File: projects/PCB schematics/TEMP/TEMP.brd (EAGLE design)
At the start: 58.4 x 54.6 mm, 17 parts, among them J1 SAMTEC-TFM-120-02-X-D-LCJ, X1 5566-4, X2 5566-4, X3 5566-2, X4 5566-6

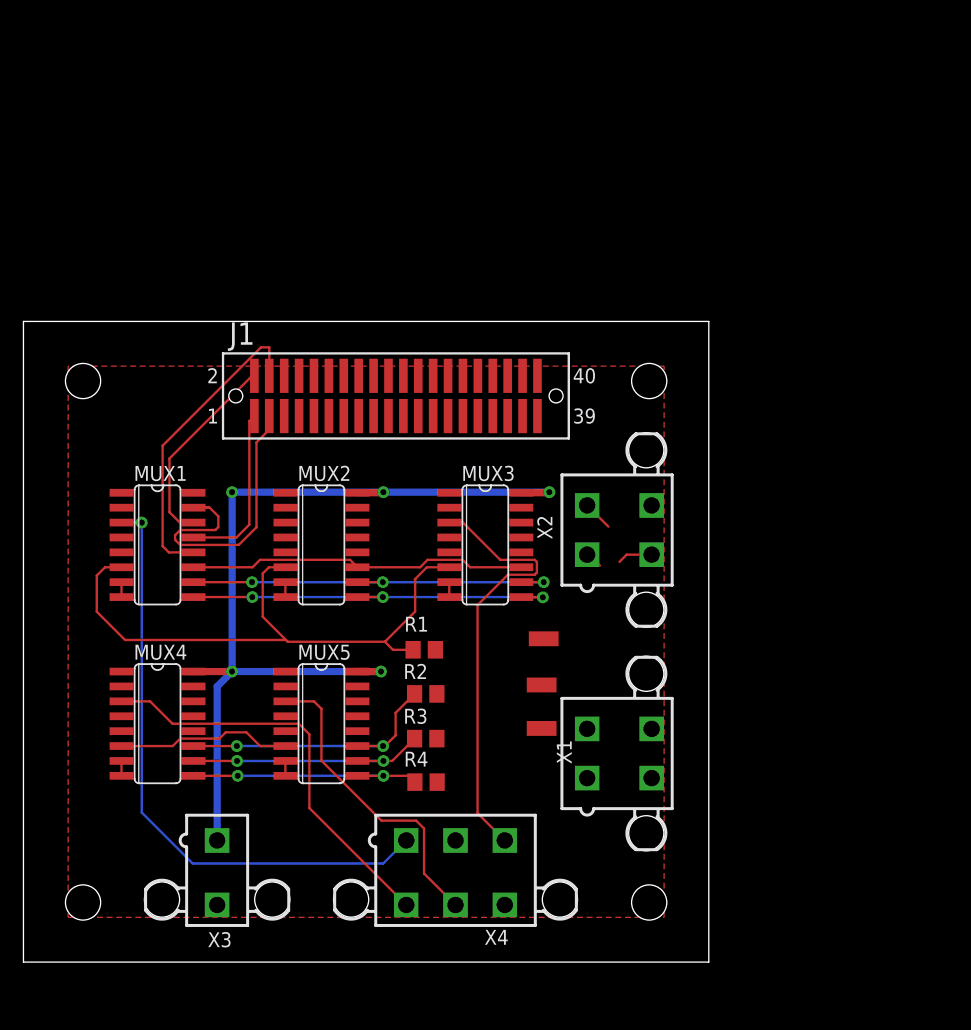
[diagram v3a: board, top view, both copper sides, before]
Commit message: TEMP - Energus components added in.
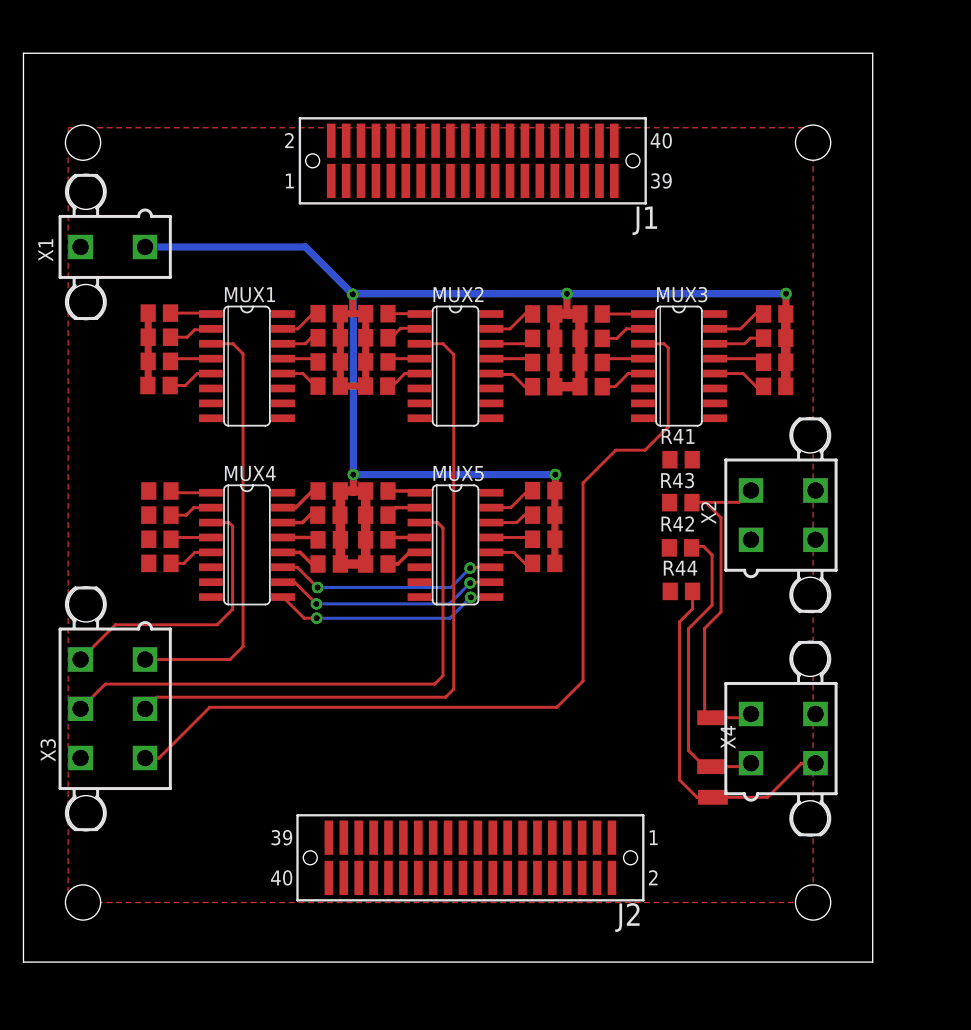
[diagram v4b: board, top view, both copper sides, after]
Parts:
- added J2: SAMTEC-TFM-120-02-X-D-LCJ, SAMTEC-TFM-120-02-X-D-LC:SAMTEC-TFM-120-02-X-D-LC
- added R10, R11, R12, R13, R14, R15, R16, R17, R18, R19, R20, R21, R22, R23, R24, R25, R26, R27, R28, R29, R30, R31, R32, R33, R34, R35, R36, R37, R38, R39, R40, R5, R6, R7, R8, R9: 680, rcl:R0805
- added R41, R42, R43, R44: 50k, rcl:R0805
- R1, R2, R3, R4: value 50k -> 680
- X1: value 5566-4 -> 5566-2; device con-molex:5566-4 -> con-molex:5566-2
- X3: value 5566-2 -> 5566-6; device con-molex:5566-2 -> con-molex:5566-6
- X4: value 5566-6 -> 5566-4; device con-molex:5566-6 -> con-molex:5566-4
- moved X1 61.1 mm to (7.62, 61.0), turned to 90 degrees
- moved R3 37.1 mm to (26.1, 55.3)
- moved R4 34.8 mm to (26.1, 49.1)
- moved R2 31.4 mm to (26.1, 53.2)
- moved X4 30.2 mm to (64.8, 19.1), turned to 270 degrees
- moved R1 25.8 mm to (26.1, 51.2)
- moved MUX3 22.5 mm to (55.9, 50.8)
- moved J1 21.1 mm to (38.3, 68.3)
- moved MUX5 19.1 mm to (36.8, 35.6)
- moved MUX2 19.0 mm to (36.8, 50.8)
- moved SH1 18.0 mm to (58.7, 16.7), turned to 180 degrees
- moved MUX4 17.0 mm to (19.1, 35.6)
- moved MUX1 17.0 mm to (19.1, 50.8)
- moved X3 16.6 mm to (7.62, 21.6), turned to 90 degrees
- moved SH3 15.7 mm to (58.8, 14.0), turned to 180 degrees
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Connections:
- net CS_A_IN: now also R42.2; no longer R2.2
- net CS_A_OUT: now also X4.1; no longer X1.1
- net CS_B_IN: now also R43.2; no longer R3.2
- net CS_B_OUT: now also X4.2; no longer X1.2
- net CS_C_IN: now also R44.2; no longer R4.2
- net CS_C_OUT: now also X4.3; no longer X1.3
- net GND: now also J1.10, J1.12, J1.14, J1.16, J1.18, J1.2, J1.20, J1.22, J1.24, J1.26, J1.28, J1.30, J1.32, J1.34, J1.36, J1.38, J1.4, J1.40, J1.6, J1.8, J2.10, J2.12, J2.14, J2.16, J2.18, J2.2, J2.20, J2.22, J2.24, J2.26, J2.28, J2.30, J2.32, J2.34, J2.36, J2.38, J2.4, J2.40, J2.6, J2.8, R41.1, R42.1, R43.1, R44.1, X1.2; no longer R1.1, R2.1, R3.1, R4.1, X3.2
- net INH: now also R41.2; no longer R1.2
- net TEMP1: now also R1.2
- net TEMP10: now also J1.19, R10.2; no longer J1.10
- net TEMP11: now also J1.21, R11.2; no longer J1.11
- net TEMP12: now also J1.23, R12.2; no longer J1.12
- net TEMP13: now also J1.25, R13.2; no longer J1.13
- net TEMP14: now also J1.27, R14.2; no longer J1.14
- net TEMP15: now also J1.29, R15.2; no longer J1.15
- net TEMP16: now also J1.31, R16.2; no longer J1.16
- net TEMP17: now also J1.33, R17.2; no longer J1.17
- net TEMP18: now also J1.35, R18.2; no longer J1.18
- net TEMP19: now also J1.37, R19.2; no longer J1.19
- net TEMP2: now also J1.3, R2.2; no longer J1.2
- net TEMP20: now also J1.39, R20.2; no longer J1.20
- net TEMP21: now also J2.1, R21.2; no longer J1.21
- net TEMP22: now also J2.3, R22.2; no longer J1.22
- net TEMP23: now also J2.5, R23.2; no longer J1.23
- net TEMP24: now also J2.7, R24.2; no longer J1.24
- net TEMP25: now also J2.9, R25.2; no longer J1.25
- net TEMP26: now also J2.11, R26.2; no longer J1.26
- net TEMP27: now also J2.13, R27.2; no longer J1.27
- net TEMP28: now also J2.15, R28.2; no longer J1.28
- net TEMP29: now also J2.17, R29.2; no longer J1.29
- net TEMP3: now also J1.5, R3.2; no longer J1.3
- net TEMP30: now also J2.19, R30.2; no longer J1.30
- net TEMP31: now also J2.21, R31.2; no longer J1.31
- net TEMP32: now also J2.23, R32.2; no longer J1.32
- net TEMP33: now also J2.25, R33.2; no longer J1.33
- net TEMP34: now also J2.27, R34.2; no longer J1.34
- net TEMP35: now also J2.29, R35.2; no longer J1.35
- net TEMP36: now also J2.31, R36.2; no longer J1.36
- net TEMP37: now also J2.33, R37.2; no longer J1.37
- net TEMP38: now also J2.35, R38.2; no longer J1.38
- net TEMP39: now also J2.37, R39.2; no longer J1.39
- net TEMP4: now also J1.7, R4.2; no longer J1.4
- net TEMP40: now also J2.39, R40.2; no longer J1.40
- net TEMP5: now also J1.9, R5.2; no longer J1.5
- net TEMP6: now also J1.11, R6.2; no longer J1.6
- net TEMP7: now also J1.13, R7.2; no longer J1.7
- net TEMP8: now also J1.15, R8.2; no longer J1.8
- net TEMP9: now also J1.17, R9.2; no longer J1.9
- net TEMP_OUT1: now also X3.1; no longer X4.1
- net TEMP_OUT2: now also X3.2; no longer X4.2
- net TEMP_OUT3: now also X3.3; no longer X4.3
- net TEMP_OUT4: now also X3.4; no longer X4.4
- net TEMP_OUT5: now also X3.5; no longer X4.5
- net VCC: now also R1.1, R10.1, R11.1, R12.1, R13.1, R14.1, R15.1, R16.1, R17.1, R18.1, R19.1, R2.1, R20.1, R21.1, R22.1, R23.1, R24.1, R25.1, R26.1, R27.1, R28.1, R29.1, R3.1, R30.1, R31.1, R32.1, R33.1, R34.1, R35.1, R36.1, R37.1, R38.1, R39.1, R4.1, R40.1, R5.1, R6.1, R7.1, R8.1, R9.1, X1.1; no longer X3.1
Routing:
- net VCC: track 80.5 -> 165.6 mm
- net INH: track 67.2 -> 0.00 mm
- net TEMP_OUT2: track 0.00 -> 58.8 mm
- net TEMP_OUT3: track 37.0 -> 75.2 mm
- net TEMP4: track 26.4 -> 3.43 mm
- net TEMP3: track 25.9 -> 3.52 mm
- net TEMP_OUT5: track 26.5 -> 46.9 mm
- net CS_C_IN: track 58.1 -> 38.6 mm, vias 5 -> 2
- net CS_B_IN: track 59.1 -> 44.3 mm, vias 5 -> 2
- net TEMP_OUT1: track 51.6 -> 36.9 mm, vias 1 -> 0
- net TEMP2: track 17.2 -> 3.20 mm
- net CS_A_IN: track 54.4 -> 40.7 mm
- net TEMP1: track 14.6 -> 3.10 mm
- net TEMP_OUT4: track 35.1 -> 23.8 mm
- net CS_C_OUT: track 0.00 -> 9.31 mm
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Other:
- board size 58.4 x 54.6 mm -> 72.4 x 77.5 mm

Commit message: TEMP - Initial board placement; Horizontal redo.
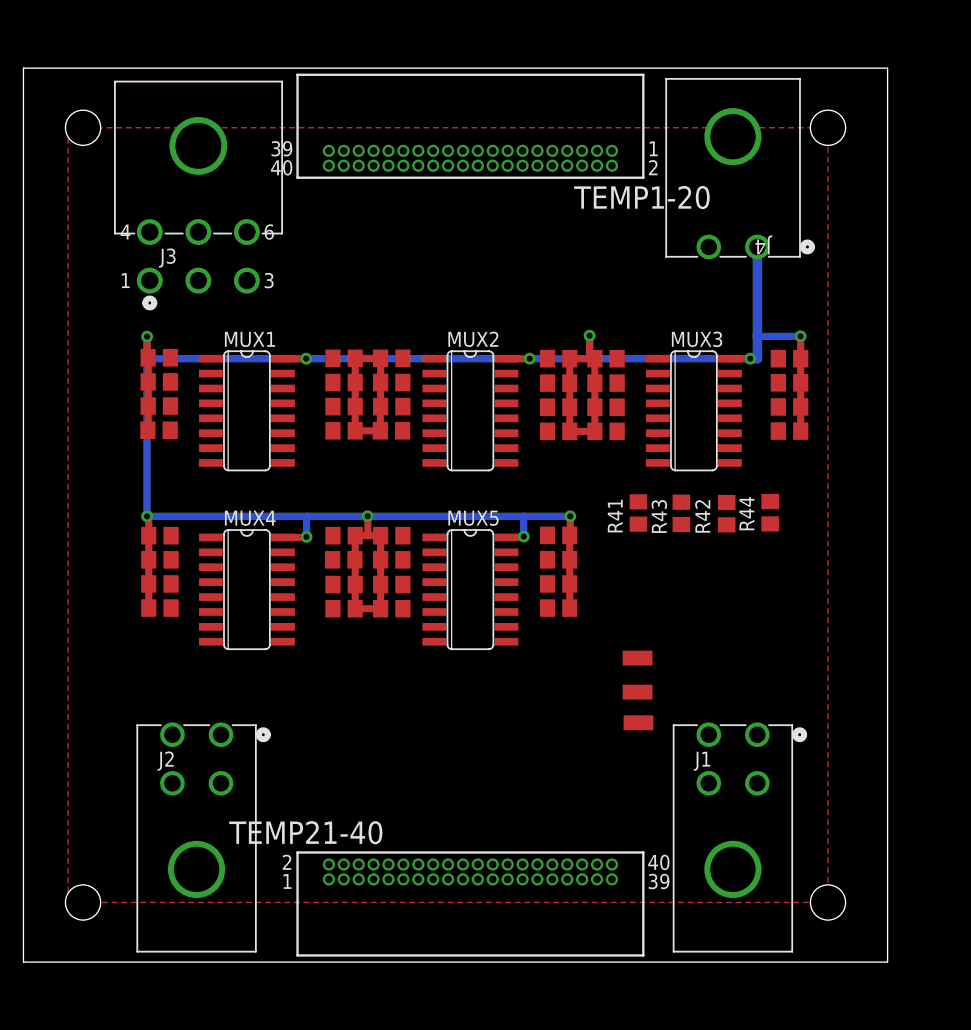
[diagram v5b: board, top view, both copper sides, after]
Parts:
- removed X1: 5566-2, con-molex:5566-2
- removed X2, X4: 5566-4, con-molex:5566-4
- removed X3: 5566-6, con-molex:5566-6
- added J3: 1-770969-0, IowaFormula:CON6_2X3_P163_RAMNL
- added J4: 770966-1, IowaFormula:CONN2_770966-1
- added TEMP1-20, TEMP21-40: SAMTEC-TFM-120-01-X-D-RA, SAMTEC-TFM-120-01-X-D-RA:SAMTEC-TFM-120-01-X-D-RA
- J1, J2: value SAMTEC-TFM-120-02-X-D-LCJ -> 770968-1; device SAMTEC-TFM-120-02-X-D-LC:SAMTEC-TFM-120-02-X-D-LC -> IowaFormula:CONN4_770968-1
- moved J1 56.7 mm to (58.4, 15.2)
- moved J2 26.2 mm to (12.7, 15.2), turned to 0 degrees
- moved R44 10.1 mm to (63.7, 38.3), turned to 90 degrees
- moved SH3 8.98 mm to (52.4, 20.4)
- moved SH1 8.98 mm to (52.3, 23.0)
- moved SH2 8.13 mm to (52.3, 25.9)
- moved R41 5.82 mm to (52.4, 38.3), turned to 90 degrees
- moved R42 4.90 mm to (59.9, 38.2), turned to 90 degrees
- moved MUX5 4.02 mm to (38.1, 31.8)
- moved R12 4.02 mm to (45.6, 45.2)
- moved R33 4.02 mm to (45.6, 32.2)
- moved R34 4.02 mm to (45.6, 34.3)
- moved R35 4.02 mm to (45.6, 36.4)
- moved R1 4.02 mm to (27.3, 47.3)
- moved R13 4.02 mm to (31.4, 51.5)
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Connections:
- net CS_A_IN: now also J1.1; no longer X2.1
- net CS_A_OUT: now also J2.1; no longer X4.1
- net CS_B_IN: now also J1.2; no longer X2.2
- net CS_B_OUT: now also J2.2; no longer X4.2
- net CS_C_IN: now also J1.3; no longer X2.3
- net CS_C_OUT: now also J2.3; no longer X4.3
- net GND: now also J4.2, TEMP1-20.10, TEMP1-20.12, TEMP1-20.14, TEMP1-20.16, TEMP1-20.18, TEMP1-20.2, TEMP1-20.20, TEMP1-20.22, TEMP1-20.24, TEMP1-20.26, TEMP1-20.28, TEMP1-20.30, TEMP1-20.32, TEMP1-20.34, TEMP1-20.36, TEMP1-20.38, TEMP1-20.4, TEMP1-20.40, TEMP1-20.6, TEMP1-20.8, TEMP21-40.10, TEMP21-40.12, TEMP21-40.14, TEMP21-40.16, TEMP21-40.18, TEMP21-40.2, TEMP21-40.20, TEMP21-40.22, TEMP21-40.24, TEMP21-40.26, TEMP21-40.28, TEMP21-40.30, TEMP21-40.32, TEMP21-40.34, TEMP21-40.36, TEMP21-40.38, TEMP21-40.4, TEMP21-40.40, TEMP21-40.6, TEMP21-40.8; no longer J1.10, J1.12, J1.14, J1.16, J1.18, J1.2, J1.20, J1.22, J1.24, J1.26, J1.28, J1.30, J1.32, J1.34, J1.36, J1.38, J1.4, J1.40, J1.6, J1.8, J2.10, J2.12, J2.14, J2.16, J2.18, J2.2, J2.20, J2.22, J2.24, J2.26, J2.28, J2.30, J2.32, J2.34, J2.36, J2.38, J2.4, J2.40, J2.6, J2.8, X1.2
- net TEMP1: now also TEMP1-20.1; no longer J1.1
- net TEMP10: now also TEMP1-20.19; no longer J1.19
- net TEMP11: now also TEMP1-20.21; no longer J1.21
- net TEMP12: now also TEMP1-20.23; no longer J1.23
- net TEMP13: now also TEMP1-20.25; no longer J1.25
- net TEMP14: now also TEMP1-20.27; no longer J1.27
- net TEMP15: now also TEMP1-20.29; no longer J1.29
- net TEMP16: now also TEMP1-20.31; no longer J1.31
- net TEMP17: now also TEMP1-20.33; no longer J1.33
- net TEMP18: now also TEMP1-20.35; no longer J1.35
- net TEMP19: now also TEMP1-20.37; no longer J1.37
- net TEMP2: now also TEMP1-20.3; no longer J1.3
- net TEMP20: now also TEMP1-20.39; no longer J1.39
- net TEMP21: now also TEMP21-40.1; no longer J2.1
- net TEMP22: now also TEMP21-40.3; no longer J2.3
- net TEMP23: now also TEMP21-40.5; no longer J2.5
- net TEMP24: now also TEMP21-40.7; no longer J2.7
- net TEMP25: now also TEMP21-40.9; no longer J2.9
- net TEMP26: now also TEMP21-40.11; no longer J2.11
- net TEMP27: now also TEMP21-40.13; no longer J2.13
- net TEMP28: now also TEMP21-40.15; no longer J2.15
- net TEMP29: now also TEMP21-40.17; no longer J2.17
- net TEMP3: now also TEMP1-20.5; no longer J1.5
- net TEMP30: now also TEMP21-40.19; no longer J2.19
- net TEMP31: now also TEMP21-40.21; no longer J2.21
- net TEMP32: now also TEMP21-40.23; no longer J2.23
- net TEMP33: now also TEMP21-40.25; no longer J2.25
- net TEMP34: now also TEMP21-40.27; no longer J2.27
- net TEMP35: now also TEMP21-40.29; no longer J2.29
- net TEMP36: now also TEMP21-40.31; no longer J2.31
- net TEMP37: now also TEMP21-40.33; no longer J2.33
- net TEMP38: now also TEMP21-40.35; no longer J2.35
- net TEMP39: now also TEMP21-40.37; no longer J2.37
- net TEMP4: now also TEMP1-20.7; no longer J1.7
- net TEMP40: now also TEMP21-40.39; no longer J2.39
- net TEMP5: now also TEMP1-20.9; no longer J1.9
- net TEMP6: now also TEMP1-20.11; no longer J1.11
- net TEMP7: now also TEMP1-20.13; no longer J1.13
- net TEMP8: now also TEMP1-20.15; no longer J1.15
- net TEMP9: now also TEMP1-20.17; no longer J1.17
- net TEMP_OUT1: now also J3.1; no longer X3.1
- net TEMP_OUT2: now also J3.2; no longer X3.2
- net TEMP_OUT3: now also J3.3; no longer X3.3
- net TEMP_OUT4: now also J3.4; no longer X3.4
- net TEMP_OUT5: now also J3.5; no longer X3.5
- net VCC: now also J4.1; no longer X1.1
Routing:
- net TEMP_OUT3: track 75.2 -> 0.00 mm
- net TEMP_OUT2: track 58.8 -> 0.00 mm
- net VCC: track 165.6 -> 216.9 mm, vias 5 -> 11
- net TEMP_OUT5: track 46.9 -> 0.00 mm
- net CS_B_IN: track 44.3 -> 0.00 mm, vias 2 -> 0
- net CS_A_IN: track 40.7 -> 0.00 mm, vias 2 -> 0
- net CS_C_IN: track 38.6 -> 0.00 mm, vias 2 -> 0
- net TEMP_OUT1: track 36.9 -> 0.00 mm
- net TEMP_OUT4: track 23.8 -> 0.00 mm
- net CS_C_OUT: track 9.31 -> 0.00 mm
- net TEMP11: track 4.91 -> 0.00 mm
- net TEMP19: track 4.66 -> 0.00 mm
- net TEMP20: track 4.58 -> 0.00 mm
- net TEMP18: track 4.33 -> 0.00 mm
- net TEMP17: track 4.26 -> 0.00 mm
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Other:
- board size 72.4 x 77.5 mm -> 73.7 x 76.2 mm

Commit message: TEMP - Final routing.
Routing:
- net CS_A_IN: track 0.00 -> 166.8 mm, vias 0 -> 4
- net CS_C_IN: track 0.00 -> 145.4 mm, vias 0 -> 4
- net GND: track 0.00 -> 132.7 mm, vias 0 -> 29
- net TEMP23: track 0.00 -> 115.0 mm, vias 0 -> 2
- net TEMP22: track 0.00 -> 113.3 mm, vias 0 -> 2
- net CS_B_IN: track 0.00 -> 107.9 mm, vias 0 -> 3
- net TEMP37: track 0.00 -> 105.9 mm, vias 0 -> 2
- net TEMP39: track 0.00 -> 103.7 mm, vias 0 -> 2
- net TEMP24: track 0.00 -> 101.0 mm, vias 0 -> 2
- net TEMP_OUT3: track 0.00 -> 97.3 mm, vias 0 -> 1
- net TEMP4: track 0.00 -> 86.1 mm, vias 0 -> 2
- net TEMP1: track 0.00 -> 82.6 mm, vias 0 -> 1
- net TEMP31: track 0.00 -> 81.7 mm, vias 0 -> 2
- net TEMP9: track 0.00 -> 81.1 mm, vias 0 -> 2
- net INH: track 0.00 -> 80.9 mm, vias 0 -> 5
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
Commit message: TEMP - Silkscreen finalization.
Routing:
- net TEMP31: track 81.7 -> 82.5 mm
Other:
- board size 73.7 x 76.2 mm -> 73.7 x 83.8 mm
- board text added: "Author: github.com/michaelpass"
- board text added: "Temperature Multiplexer (TEMP) Rev. A, April 30th, 2019"
